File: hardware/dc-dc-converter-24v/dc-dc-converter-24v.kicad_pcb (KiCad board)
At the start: 2 copper layers, 100 x 100 mm, 54 parts, among them J1 24V, J2 12V, J3 GND, J4 GND, Q1 SQJA42EP, Q2 SQJA42EP, Q3 SQJA42EP, Q4 SQJA42EP, U1 LM5176

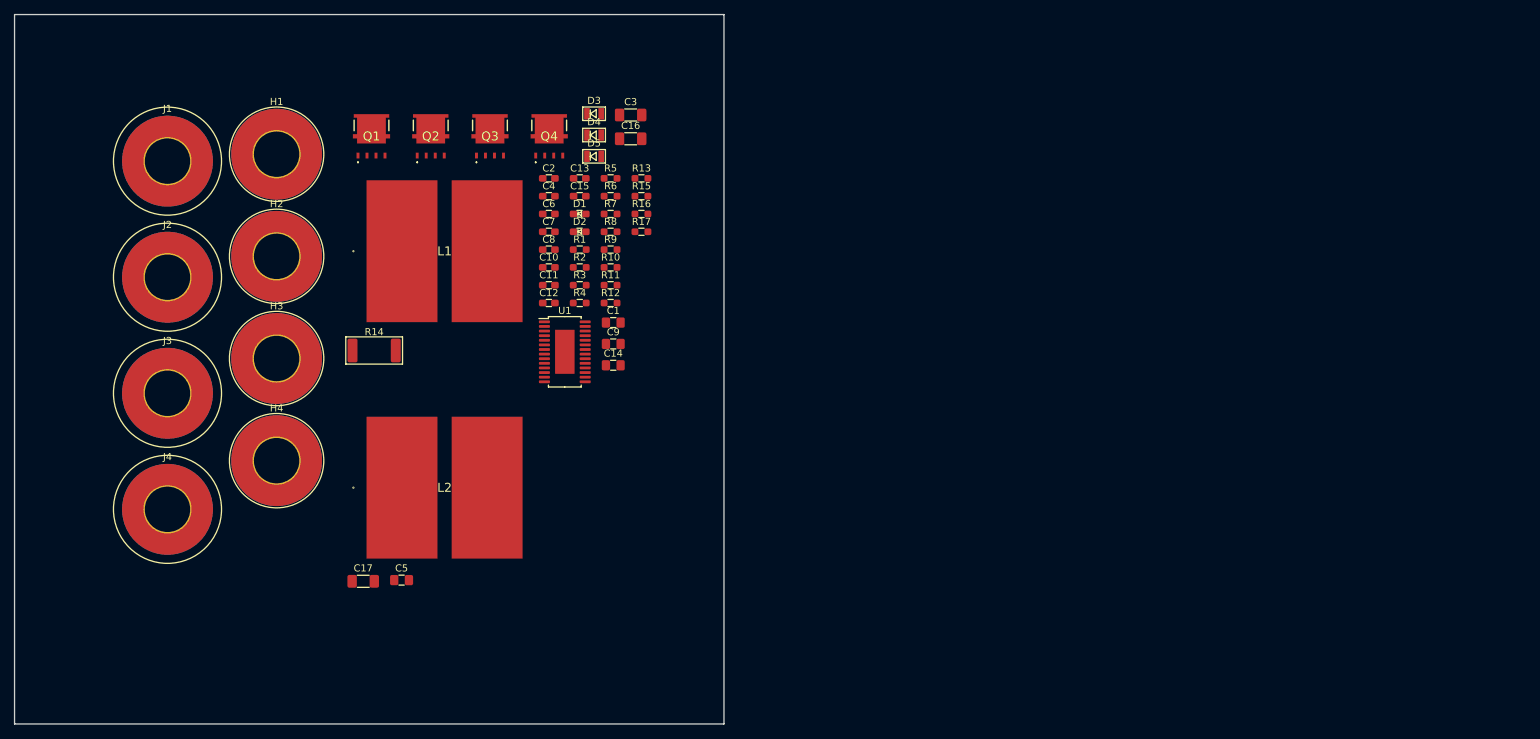
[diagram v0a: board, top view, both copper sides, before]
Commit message: create layout for DC-DC converter
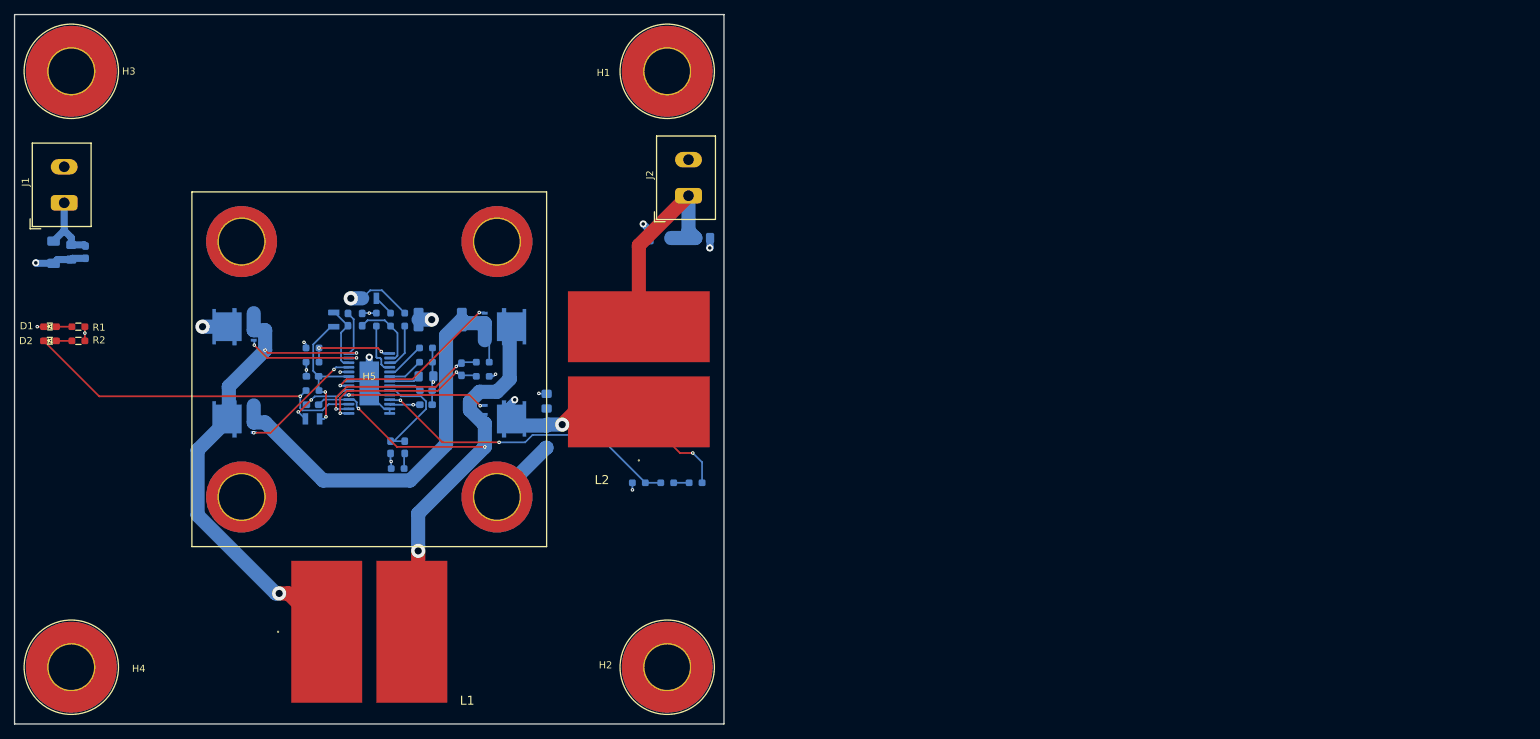
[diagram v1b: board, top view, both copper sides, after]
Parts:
- removed J3, J4: GND, benediktibk:Connector_M6
- added H5: heatsink_50x50, benediktibk:heatsink_50x50, F.Cu at (70.0, 70.0)
- C1: renamed from C2; moved to B.Cu
- C10: renamed from C11; moved to B.Cu
- C11: renamed from C12; moved to B.Cu
- C12: renamed from C16; moved to B.Cu
- C13: renamed from C15; moved to B.Cu
- C14: renamed from C1; moved to B.Cu
- C15: renamed from C3; moved to B.Cu
- C16: renamed from C5; moved to B.Cu
- C17, D3, D4, D5, R10, R11, R3, R4, R5, R6, R7, R8, R9, U1: moved to B.Cu
- C2: renamed from C4; moved to B.Cu
- C3: renamed from C6; moved to B.Cu
- C4: renamed from C7; moved to B.Cu
- C5: renamed from C8; moved to B.Cu
- C6: renamed from C9; moved to B.Cu
- C7: renamed from C10; moved to B.Cu
- C8: renamed from C13; moved to B.Cu
- C9: renamed from C14; moved to B.Cu
- J1: value 24V -> 12V; footprint benediktibk:Connector_M6 -> benediktibk:rspro_header_2pin_5_08mm
- J2: value 12V -> 24V; footprint benediktibk:Connector_M6 -> benediktibk:rspro_header_2pin_5_08mm
- Q1: renamed from Q2; moved to B.Cu
- Q2: renamed from Q1; moved to B.Cu
- Q3: renamed from Q4; moved to B.Cu
- Q4: renamed from Q3; moved to B.Cu
- R12: renamed from R15; moved to B.Cu
- R13: renamed from R16; moved to B.Cu
- R14: renamed from R17; moved to B.Cu
- R15: renamed from R12; moved to B.Cu
- R16: renamed from R13; moved to B.Cu
- R17: renamed from R14; moved to B.Cu
- moved C12 82.9 mm to (25.5, 53.5), turned to -90 degrees
- moved C9 78.0 mm to (28.0, 53.5), turned to -90 degrees
- moved D1 76.3 mm to (25.0, 64.0)
- moved D2 76.2 mm to (25.0, 66.0)
- moved J2 74.8 mm to (115.0, 43.0), turned to 90 degrees
- moved R1 71.5 mm to (29.0, 64.0), turned to 180 degrees
- moved R2 71.4 mm to (29.0, 66.0), turned to 180 degrees
- moved C8 70.4 mm to (30.0, 53.5), turned to -90 degrees
- moved C16 64.2 mm to (117.0, 51.5)
- moved C17 64.0 mm to (111.0, 51.5), turned to 180 degrees
- moved H2 62.3 mm to (112.0, 112.0)
- moved H1 60.9 mm to (112.0, 28.0)
- moved L1 54.7 mm to (70.0, 107.0)
- moved D5 54.3 mm to (62.0, 77.0)
- moved H4 52.3 mm to (28.0, 112.0)
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- renumbered H2 to H1, H4 to H2, H1 to H3, H3 to H4
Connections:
- C11 pad 2: Net-(Q3-G) (its old number) -> Net-(Q3-S)
- J1 pad 1: /Output Filter/24VFILT -> /Boost Converter/12V
- J2 pad 1: /Boost Converter/12V -> /Output Filter/24VFILT
- L1 pad 2: Net-(Q3-D) -> Net-(Q3-S)
- Q3 pad 1: Net-(Q3-D) -> Net-(Q3-S)
- Q4 pad 2: Net-(Q3-G) (its old number) -> Net-(Q4-G)
- Q4 pad 3: Net-(Q3-D) -> Net-(Q3-S)
- U1 pad 18: Net-(Q3-G) (its old number) -> Net-(Q3-S)
- U1 pad 21: unconnected-(U1-LDRV2-Pad21) -> Net-(Q4-G)
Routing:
- net Net-(Q1-S): track 0.00 -> 79.4 mm, vias 0 -> 3
- net Net-(Q3-S): track 0.00 -> 78.9 mm, vias 0 -> 3
- net /Boost Converter/Vout: track 0.00 -> 72.4 mm, vias 0 -> 5
- net Net-(Q2-S): track 0.00 -> 62.7 mm
- net GND: track 0.00 -> 57.3 mm, vias 0 -> 13
- net Net-(D2-K): track 0.00 -> 49.5 mm, vias 0 -> 1
- net Net-(U1-FB): track 0.00 -> 43.9 mm, vias 0 -> 2
- net /Output Filter/24VFILT: track 0.00 -> 31.1 mm
- net /Boost Converter/12V: track 0.00 -> 26.5 mm, vias 0 -> 4
- net Net-(Q4-G): track 0.00 -> 25.9 mm, vias 0 -> 2
- net Net-(U1-CS): track 0.00 -> 25.3 mm, vias 0 -> 2
- net Net-(U1-CSG): track 0.00 -> 24.3 mm, vias 0 -> 2
- net /Boost Converter/Vcc: track 0.00 -> 20.6 mm, vias 0 -> 2
- net Net-(Q3-G): track 0.00 -> 19.8 mm, vias 0 -> 2
- net Net-(Q2-G): track 0.00 -> 17.2 mm, vias 0 -> 2
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- added copper zone on In1.Cu, net /Boost Converter/12V
- added copper zone on In2.Cu, net GND
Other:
- copper layers 2 -> 4

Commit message: add version on silkscreen
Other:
- board text added: "DC-DC Converter 24V R01"
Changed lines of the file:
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@@
   (gr_rect (start 20 20) (end 120 120)
     (stroke (width 0.1) (type default)) (fill none) (layer "Edge.Cuts"))
+  (gr_text "DC-DC Converter 24V R01" (at 61 26) (layer "F.SilkS")
+    (effects (font (size 1.5 1.5) (thickness 0.3) bold) (justify left bottom))
+  )
   (segment (start 113.8 81.8) (end 108 76) (width 0.25) (layer "F.Cu") (net 1))
   (segment (start 115.6 81.8) (end 113.8 81.8) (width 0.25) (layer "F.Cu") (net 1))

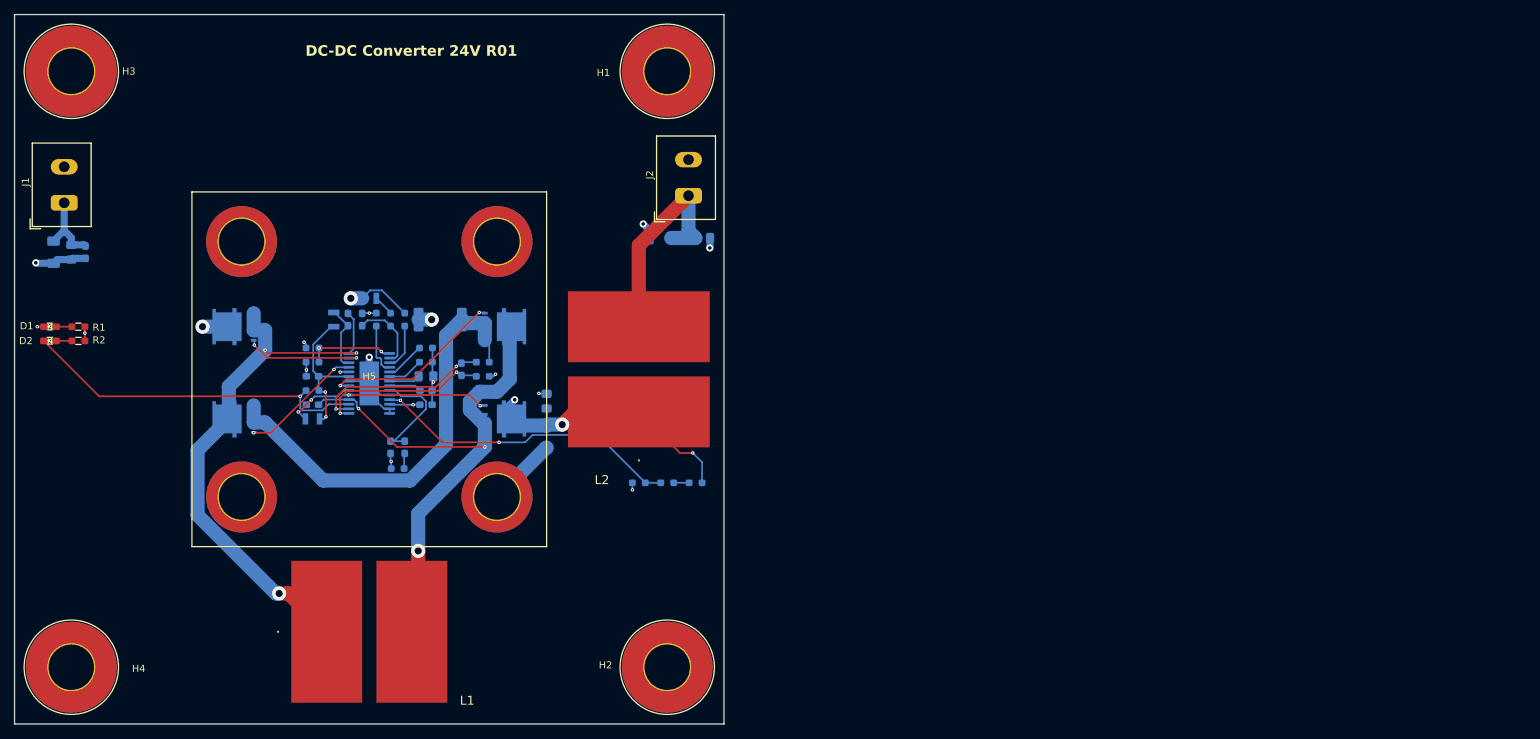
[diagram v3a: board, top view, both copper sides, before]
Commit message: start with redesign of DC DC converter
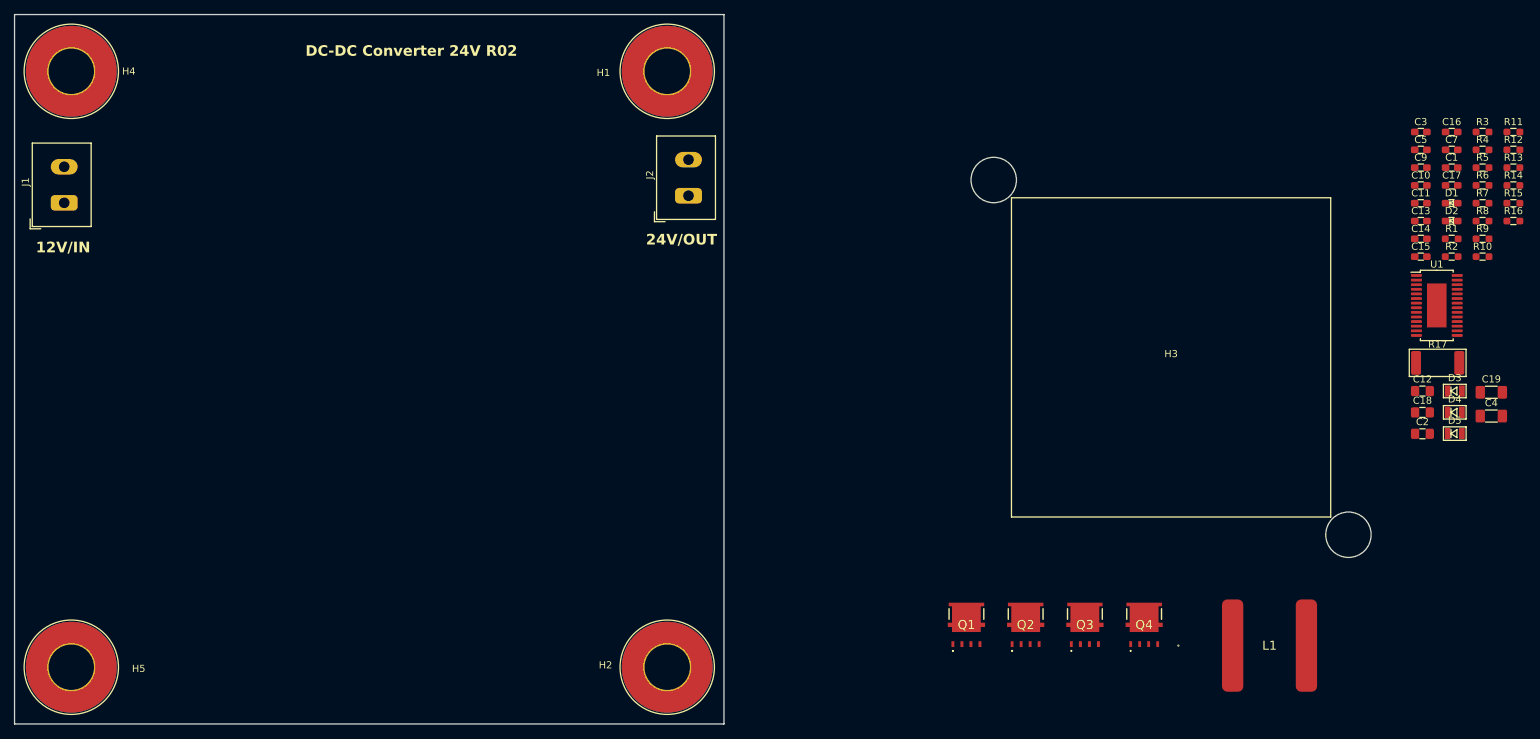
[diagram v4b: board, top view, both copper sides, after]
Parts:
- removed C6: 240pF, benediktibk:C_0805_2012Metric_Pad1.18x1.45mm_HandSolder
- removed C8: 1uF, benediktibk:C_0603_1608Metric_Pad1.08x0.95mm_HandSolder
- removed the H5 at (70.0, 70.0)
- removed L2: 2.5µH, benediktibk:ETQP8
- added C18: 4.7uF, benediktibk:C_0805_2012Metric_Pad1.18x1.45mm_HandSolder, F.Cu at (218.5, 76.1)
- added C19: 47uF, benediktibk:C_1206_3216Metric_Pad1.33x1.80mm_HandSolder, F.Cu at (228.2, 73.2)
- added H3: heatsink_ATS-CPX045045035-164-C2-R0, benediktibk:heatsink_984-CPX04504-164C2R0, F.Cu at (183.0, 68.3)
- C1: value 100nF -> 1uF; moved to F.Cu
- C10, D3, D4, D5, Q1, Q2, Q3, Q4, R10, R11, R12, R13, R14, R15, R16, R17, R3, R4, R5, R6, R7, R8, R9, U1: moved to F.Cu
- C11: value 100nF -> 560pF; moved to F.Cu
- C12: value 47uF -> 240pF; footprint benediktibk:C_1206_3216Metric_Pad1.33x1.80mm_HandSolder -> benediktibk:C_0805_2012Metric_Pad1.18x1.45mm_HandSolder; moved to F.Cu
- C13: value 47pF -> 33nF; moved to F.Cu
- C14: value 4.7uF -> 100nF; footprint benediktibk:C_0805_2012Metric_Pad1.18x1.45mm_HandSolder -> benediktibk:C_0603_1608Metric_Pad1.08x0.95mm_HandSolder; moved to F.Cu
- C15: value 47uF -> 100nF; footprint benediktibk:C_1206_3216Metric_Pad1.33x1.80mm_HandSolder -> benediktibk:C_0603_1608Metric_Pad1.08x0.95mm_HandSolder; moved to F.Cu
- C16: value 4.7uF -> 47pF; footprint benediktibk:C_0805_2012Metric_Pad1.18x1.45mm_HandSolder -> benediktibk:C_0603_1608Metric_Pad1.08x0.95mm_HandSolder; moved to F.Cu
- C17: value 47uF -> 1uF; footprint benediktibk:C_1206_3216Metric_Pad1.33x1.80mm_HandSolder -> benediktibk:C_0603_1608Metric_Pad1.08x0.95mm_HandSolder; moved to F.Cu
- C2: value 100nF -> 4.7uF; footprint benediktibk:C_0603_1608Metric_Pad1.08x0.95mm_HandSolder -> benediktibk:C_0805_2012Metric_Pad1.18x1.45mm_HandSolder; moved to F.Cu
- C3: value 1uF -> 100nF; moved to F.Cu
- C4: value 100nF -> 47uF; footprint benediktibk:C_0603_1608Metric_Pad1.08x0.95mm_HandSolder -> benediktibk:C_1206_3216Metric_Pad1.33x1.80mm_HandSolder; moved to F.Cu
- C5: value 560pF -> 100nF; moved to F.Cu
- C7: value 33nF -> 100nF; moved to F.Cu
- C9: value 4.7uF -> 1uF; footprint benediktibk:C_0805_2012Metric_Pad1.18x1.45mm_HandSolder -> benediktibk:C_0603_1608Metric_Pad1.08x0.95mm_HandSolder; moved to F.Cu
- moved D1 198.3 mm to (222.6, 46.6)
- moved D2 198.3 mm to (222.6, 49.1)
- moved R1 194.0 mm to (222.6, 51.6), turned to 0 degrees
- moved C12 193.9 mm to (218.5, 73.1), turned to 0 degrees
- moved R2 193.9 mm to (222.6, 54.1), turned to 0 degrees
- moved C9 190.6 mm to (218.2, 41.6), turned to 0 degrees
- moved R3 168.9 mm to (226.9, 36.6), turned to 0 degrees
- moved R6 166.5 mm to (226.9, 44.1)
- moved R7 166.4 mm to (226.9, 46.6), turned to 0 degrees
- moved R11 164.3 mm to (231.3, 36.6), turned to 0 degrees
- moved D5 161.0 mm to (223.0, 79.1)
- moved C3 160.0 mm to (218.2, 36.6), turned to 0 degrees
- moved C4 159.7 mm to (228.2, 76.6), turned to 0 degrees
- moved C11 158.8 mm to (218.2, 46.6)
- moved D4 158.5 mm to (223.0, 76.1), turned to 0 degrees
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- renumbered H3 to H4, H4 to H5
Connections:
- C1 pad 1: /Boost Converter/Vout -> /Vin
- C10 pad 1: Net-(D4-K) -> Net-(U1-VIN)
- C10 pad 2: Net-(Q1-S) -> GND
- C11 pad 1: Net-(D5-K) -> Net-(U1-COMP)
- C11 pad 2: Net-(Q3-S) -> GND
- C12 pad 1: /Boost Converter/12V -> Net-(U1-SLOPE)
- C13 pad 1: Net-(U1-CS) -> Net-(U1-COMP)
- C13 pad 2: Net-(U1-CSG) -> Net-(C13-Pad2)
- C14 pad 1: /Boost Converter/Vout -> Net-(D4-K)
- C14 pad 2: GND -> Net-(Q1-S)
- C15 pad 1: /Boost Converter/Vout -> Net-(D5-K)
- C15 pad 2: GND -> Net-(Q3-S)
- C16 pad 1: /Output Filter/24VFILT -> Net-(U1-CS)
- C16 pad 2: GND -> Net-(U1-CSG)
- C17 pad 1: /Output Filter/24VFILT -> /Vout
- C2 pad 1: Net-(U1-SS) -> /Vin
- C3 pad 1: /Boost Converter/Vcc -> Net-(U1-BIAS)
- C4 pad 1: Net-(U1-VIN) -> /Vin
- C5 pad 1: Net-(U1-COMP) -> Net-(U1-SS)
- C7 pad 1: Net-(U1-COMP) -> Net-(U1-EN/UVLO)
- C7 pad 2: Net-(C7-Pad2) -> GND
- C9 pad 1: /Boost Converter/12V -> /Vcc
- D3 pad 2: /Boost Converter/12V -> /Vin
- D4 pad 2: /Boost Converter/Vcc -> /Vcc
- D5 pad 2: /Boost Converter/Vcc -> /Vcc
- H1 pad 1: unconnected-(H1-Pad1) -> GND
- H2 pad 1: unconnected-(H2-Pad1) -> GND
- H4 pad 1: unconnected-(H3-Pad1) -> GND
- H5 pad 1: unconnected-(H4-Pad1) -> GND
- J1 pad 1: /Boost Converter/12V -> /Vin
- J2 pad 1: /Output Filter/24VFILT -> /Vout
- Q1 pad 3: /Boost Converter/12V -> /Vin
- Q3 pad 3: /Boost Converter/Vout -> /Vout
- R1 pad 1: /Boost Converter/12V -> /Vin
- R11 pad 1: Net-(C7-Pad2) -> Net-(C13-Pad2)
- R13 pad 1: /Boost Converter/Vout -> /Vout
- R2 pad 1: /Boost Converter/12V -> /Vin
- R3 pad 1: /Boost Converter/Vcc -> /Vcc
- R6 pad 1: /Boost Converter/12V -> /Vin
- R9 pad 1: /Boost Converter/12V -> /Vin
- U1 pad 12: /Boost Converter/Vout -> /Vout
- U1 pad 23: /Boost Converter/Vcc -> /Vcc
- U1 pad 24: /Boost Converter/Vout -> Net-(U1-BIAS)
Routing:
- net Net-(Q1-S): track 79.4 -> 0.00 mm, vias 3 -> 0
- net Net-(Q3-S): track 78.9 -> 0.00 mm, vias 3 -> 0
- net /Boost Converter/Vout: track 72.4 -> 0.00 mm, vias 5 -> 0
- net Net-(Q2-S): track 62.7 -> 0.00 mm
- net GND: track 57.3 -> 0.00 mm, vias 13 -> 0
- net Net-(D2-K): track 49.5 -> 0.00 mm, vias 1 -> 0
- net Net-(U1-FB): track 43.9 -> 0.00 mm, vias 2 -> 0
- net /Output Filter/24VFILT: track 31.1 -> 0.00 mm
- net /Boost Converter/12V: track 26.5 -> 0.00 mm, vias 4 -> 0
- net Net-(Q4-G): track 25.9 -> 0.00 mm, vias 2 -> 0
- net Net-(U1-CS): track 25.3 -> 0.00 mm, vias 2 -> 0
- net Net-(U1-CSG): track 24.3 -> 0.00 mm, vias 2 -> 0
- net /Boost Converter/Vcc: track 20.6 -> 0.00 mm, vias 2 -> 0
- net Net-(Q3-G): track 19.8 -> 0.00 mm, vias 2 -> 0
- net Net-(Q2-G): track 17.2 -> 0.00 mm, vias 2 -> 0
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- removed copper zone on In1.Cu, net /Boost Converter/12V
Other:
- board text added: "12V/IN"
- board text added: "24V/OUT"
- board text added: "DC-DC Converter 24V R02"
- board text removed: "DC-DC Converter 24V R01"

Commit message: layout DC DC converter
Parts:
- added C20: 470uF, benediktibk:PCAP_16x16_5-ELECT_NCA-M, F.Cu at (108.0, 85.0)
- added C21: 4700uF, benediktibk:CP_Radial_D22.0mm_P10.00mm_SnapIn, F.Cu at (102.0, 63.0)
- added C6: 470uF, benediktibk:PCAP_16x16_5-ELECT_NCA-M, F.Cu at (32.0, 85.0)
- added C8: 4700uF, benediktibk:CP_Radial_D22.0mm_P10.00mm_SnapIn, F.Cu at (38.0, 63.0)
- C1, C10, C11, C12, C13, C14, C15, C16, C17, C18, C19, C2, C3, C4, C5, C7, C9, D3, D4, D5, L1, Q1, Q2, Q3, Q4, R1, R10, R11, R12, R13, R14, R15, R16, R17, R2, R3, R4, R5, R6, R7, R8, R9, U1: moved to B.Cu
- moved C4 198.0 mm to (33.0, 43.0), turned to 90 degrees
- moved C2 186.0 mm to (36.0, 43.0), turned to 90 degrees
- moved C1 183.6 mm to (39.0, 43.0), turned to 90 degrees
- moved R6 180.0 mm to (47.0, 39.0)
- moved R1 177.4 mm to (46.0, 35.0), turned to 90 degrees
- moved D1 177.3 mm to (46.0, 31.0), turned to -90 degrees
- moved R7 176.1 mm to (51.0, 39.0)
- moved R2 173.6 mm to (50.0, 35.0), turned to 90 degrees
- moved D2 173.5 mm to (50.0, 31.0), turned to -90 degrees
- moved R16 171.7 mm to (67.0, 99.0), turned to 90 degrees
- moved D3 168.5 mm to (56.0, 51.0), turned to 180 degrees
- moved R10 168.4 mm to (58.5, 52.0), turned to -90 degrees
- moved R15 166.7 mm to (73.0, 99.0), turned to 90 degrees
- moved R9 163.9 mm to (63.0, 52.0), turned to -90 degrees
- moved C7 163.1 mm to (60.0, 52.0), turned to 90 degrees
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- renumbered H4 to H3, H5 to H4, H3 to H5
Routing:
- net GND: track 0.00 -> 53.7 mm, vias 0 -> 34
- net Net-(Q1-S): track 0.00 -> 52.8 mm, vias 0 -> 40
- net Net-(Q3-S): track 0.00 -> 52.3 mm, vias 0 -> 42
- net Net-(D2-K): track 0.00 -> 50.3 mm, vias 0 -> 1
- net Net-(U1-CS): track 0.00 -> 42.5 mm, vias 0 -> 2
- net Net-(U1-CSG): track 0.00 -> 42.5 mm, vias 0 -> 4
- net Net-(Q4-G): track 0.00 -> 38.6 mm, vias 0 -> 2
- net Net-(Q2-S): track 0.00 -> 36.4 mm, vias 0 -> 3
- net Net-(Q2-G): track 0.00 -> 35.9 mm, vias 0 -> 2
- net /Vin: track 0.00 -> 34.4 mm, vias 0 -> 24
- net /Vout: track 0.00 -> 31.3 mm, vias 0 -> 24
- net Net-(U1-EN/UVLO): track 0.00 -> 31.3 mm
- net Net-(Q1-G): track 0.00 -> 18.4 mm
- net Net-(Q3-G): track 0.00 -> 13.1 mm
- net Net-(U1-VIN): track 0.00 -> 10.9 mm
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- added copper zone on In1.Cu, net /Vcc
- added copper zone on F.Cu, net /Vin
- added copper zone on In1.Cu, net /Vin
- added copper zone on F.Cu, net /Vout
- added copper zone on In1.Cu, net /Vout
- added copper zone on F.Cu, net GND
- added copper zone on F.Cu, net Net-(Q1-S)
- added copper zone on F.Cu, net Net-(Q2-S)
- added copper zone on F.Cu, net Net-(Q3-S)
